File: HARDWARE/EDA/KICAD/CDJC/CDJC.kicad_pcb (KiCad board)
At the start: 2 copper layers, 116.2 x 101.5 mm, 63 parts, among them J1 COM_IN, J2 COM_OUT, J3 POWER_IN, J4 POWER_OUT, J5 BIT_OUT, Q1 BC549, SW1 B-SET, U1 74LS04, U2 74LS32, U3 74LS08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

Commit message: work stop
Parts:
- moved D4 262.7 mm to (-18.7, 256.6), turned to 0 degrees
- moved D5 261.7 mm to (-18.7, 252.4), turned to 0 degrees
- moved D6 260.8 mm to (-18.7, 248.2), turned to 0 degrees
- moved D7 260.0 mm to (-18.7, 244.0), turned to 0 degrees
- moved D8 259.3 mm to (-18.7, 239.8), turned to 0 degrees
- moved U6 256.4 mm to (7.58, 240.5), turned to 0 degrees
- moved R7 245.5 mm to (-6.38, 256.6), turned to 180 degrees
- moved C9 245.3 mm to (15.2, 237.2), turned to 180 degrees
- moved R10 244.4 mm to (-6.38, 252.4), turned to 180 degrees
- moved R12 243.5 mm to (-6.38, 248.2), turned to 180 degrees
- moved R13 242.6 mm to (-6.38, 244.0), turned to 180 degrees
- moved R14 242.0 mm to (-6.38, 239.8), turned to 180 degrees
- moved U8 220.5 mm to (2.93, 208.3), turned to 0 degrees
- moved C3 210.3 mm to (10.6, 205.1), turned to 180 degrees
- moved U7 191.9 mm to (3.78, 177.3), turned to 0 degrees
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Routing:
- net LBLBI: track 87.5 -> 23.2 mm
- net FB_SW: track 68.2 -> 19.4 mm
- net Net-(U1-Pad13): track 44.6 -> 0.00 mm
- net Net-(U1-Pad11): track 44.2 -> 0.00 mm
- net MRI: track 62.2 -> 23.0 mm
- net FBMon: track 37.5 -> 1.13 mm
- net MRLMon: track 29.2 -> 0.00 mm, vias 1 -> 0
- net GNDD: track 168.5 -> 140.0 mm
- net EI: track 50.0 -> 22.9 mm
- net Net-(U1-Pad9): track 26.6 -> 0.00 mm
- net LB_SW: track 34.4 -> 14.8 mm, vias 1 -> 0
- net Net-(U6-Pad11): track 17.7 -> 0.00 mm
- net LBMon: track 17.3 -> 1.04 mm
- net NB_SW: track 40.2 -> 23.9 mm
- net Net-(U6-Pad2): track 9.46 -> 0.00 mm
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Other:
- board size 116.2 x 101.5 mm -> 100 x 100 mm

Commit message: adjust layout pcb
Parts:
- R1, R10, R11, R12, R13, R14, R2, R3, R4, R5, R6, R7, R8, R9: footprint Resistor_THT:R_Axial_DIN0207_L6.3mm_D2.5mm_P7.62mm_Horizontal -> Resistor_THT:R_Axial_DIN0207_L6.3mm_D2.5mm_P2.54mm_Vertical
- moved D4 264.4 mm to (206.0, 117.2), turned to 90 degrees
- moved R7 261.0 mm to (206.0, 104.9), turned to 270 degrees
- moved D5 258.7 mm to (201.8, 117.2), turned to 90 degrees
- moved R10 255.1 mm to (201.8, 104.9), turned to 270 degrees
- moved D6 252.9 mm to (197.6, 117.2), turned to 90 degrees
- moved R12 249.3 mm to (197.6, 104.9), turned to 270 degrees
- moved D7 247.1 mm to (193.4, 117.2), turned to 90 degrees
- moved R13 243.5 mm to (193.4, 104.9), turned to 270 degrees
- moved D8 241.4 mm to (189.2, 117.2), turned to 90 degrees
- moved R14 237.6 mm to (189.2, 104.9), turned to 270 degrees
- moved U6 231.0 mm to (190.9, 99.9), turned to 90 degrees
- moved C7 227.6 mm to (229.0, 76.0), turned to 180 degrees
- moved C9 225.2 mm to (187.6, 92.3), turned to 270 degrees
- moved U9 210.7 mm to (221.3, 80.0), turned to 0 degrees
- moved R1 209.4 mm to (197.2, 64.7)
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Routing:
- net GNDD: track 140.0 -> 88.8 mm
- net FB_SW: track 19.4 -> 2.35 mm
- net NB_SW: track 23.9 -> 13.2 mm
- net LB_SW: track 14.8 -> 9.97 mm
- net LBLBI: track 23.2 -> 19.7 mm
- net Net-(D3-Pad2): track 3.48 -> 0.00 mm
- net Net-(D1-Pad2): track 3.40 -> 0.00 mm
- net MRI: track 23.0 -> 19.7 mm
- net +5VD: track 54.4 -> 51.1 mm
- net EI: track 22.9 -> 19.7 mm
- net Net-(D2-Pad2): track 3.48 -> 0.41 mm
- net Net-(D7-Pad2): track 2.21 -> 0.00 mm
- net Net-(D8-Pad2): track 2.20 -> 0.00 mm
- net Net-(D6-Pad2): track 2.20 -> 0.00 mm
- net Net-(D5-Pad2): track 2.20 -> 0.00 mm
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
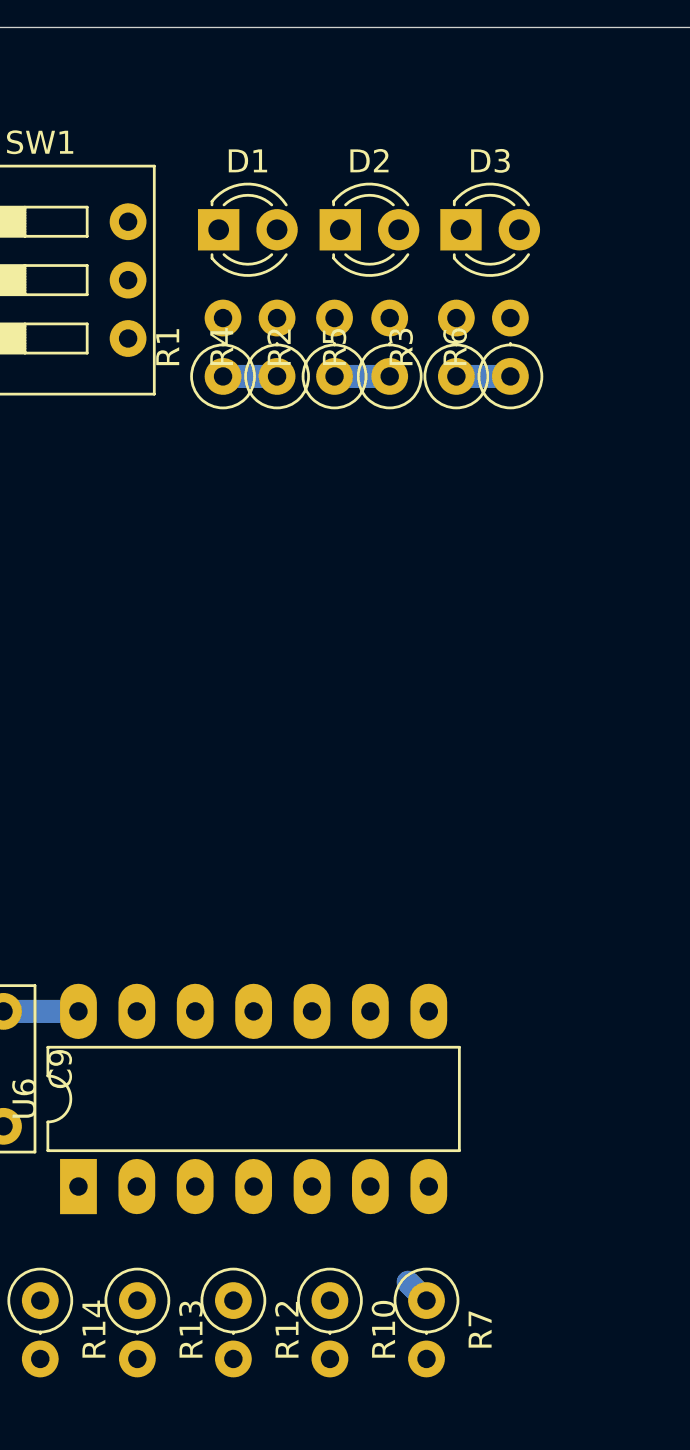
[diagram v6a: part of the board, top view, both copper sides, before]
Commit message: Adjust resitor alingment
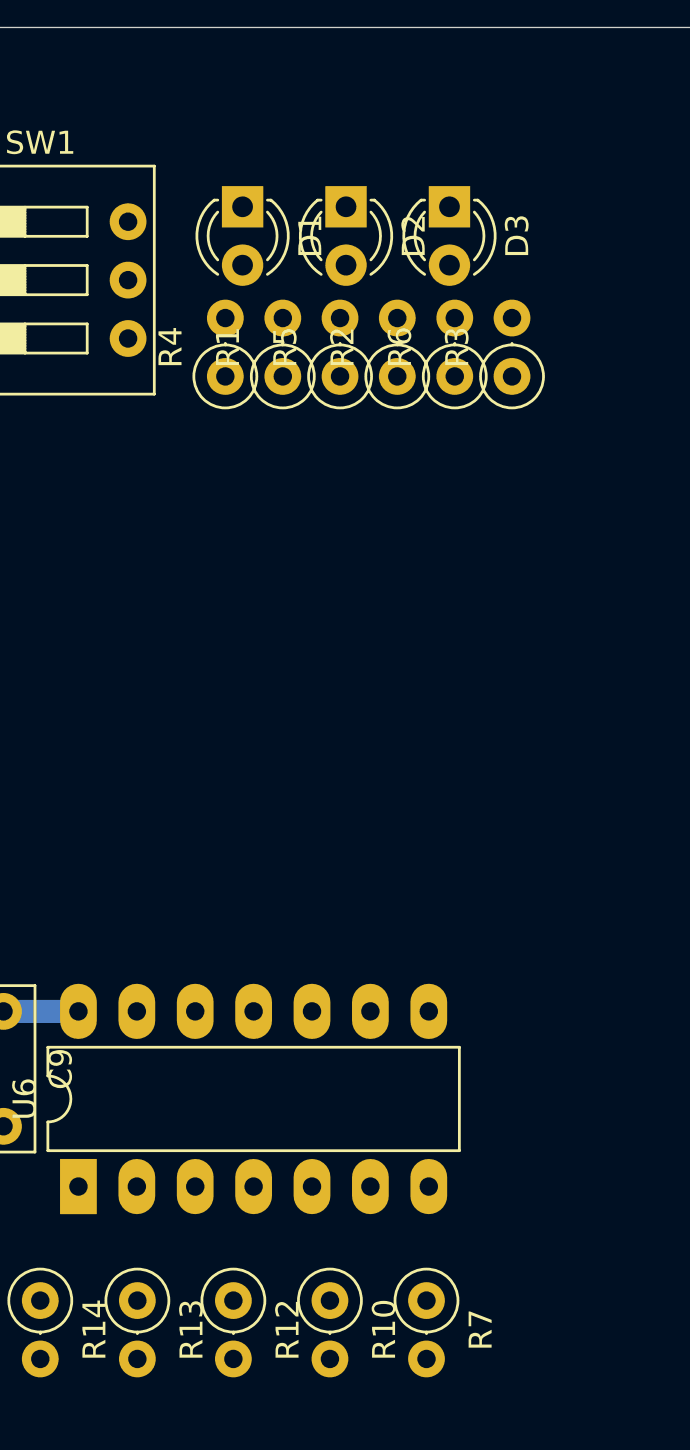
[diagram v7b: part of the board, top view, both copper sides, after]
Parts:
- moved R2 2.73 mm to (204.7, 64.7)
- moved R1 2.60 mm to (199.8, 64.7)
- moved R6 2.42 mm to (207.2, 64.7)
- moved R3 2.42 mm to (209.7, 64.7)
- moved R4 2.25 mm to (197.2, 64.7)
- moved R5 2.16 mm to (202.2, 64.7)
- moved D1 1.44 mm to (198.0, 57.3), turned to 270 degrees
- moved D3 1.12 mm to (207.0, 57.3), turned to 270 degrees
- moved D2 1.03 mm to (202.5, 57.3), turned to 270 degrees
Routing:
- net NB_SW: track 13.2 -> 10.8 mm
- net LB_SW: track 9.97 -> 7.62 mm
- net FB_SW: track 2.35 -> 0.00 mm
- net FBMon: track 1.13 -> 0.00 mm

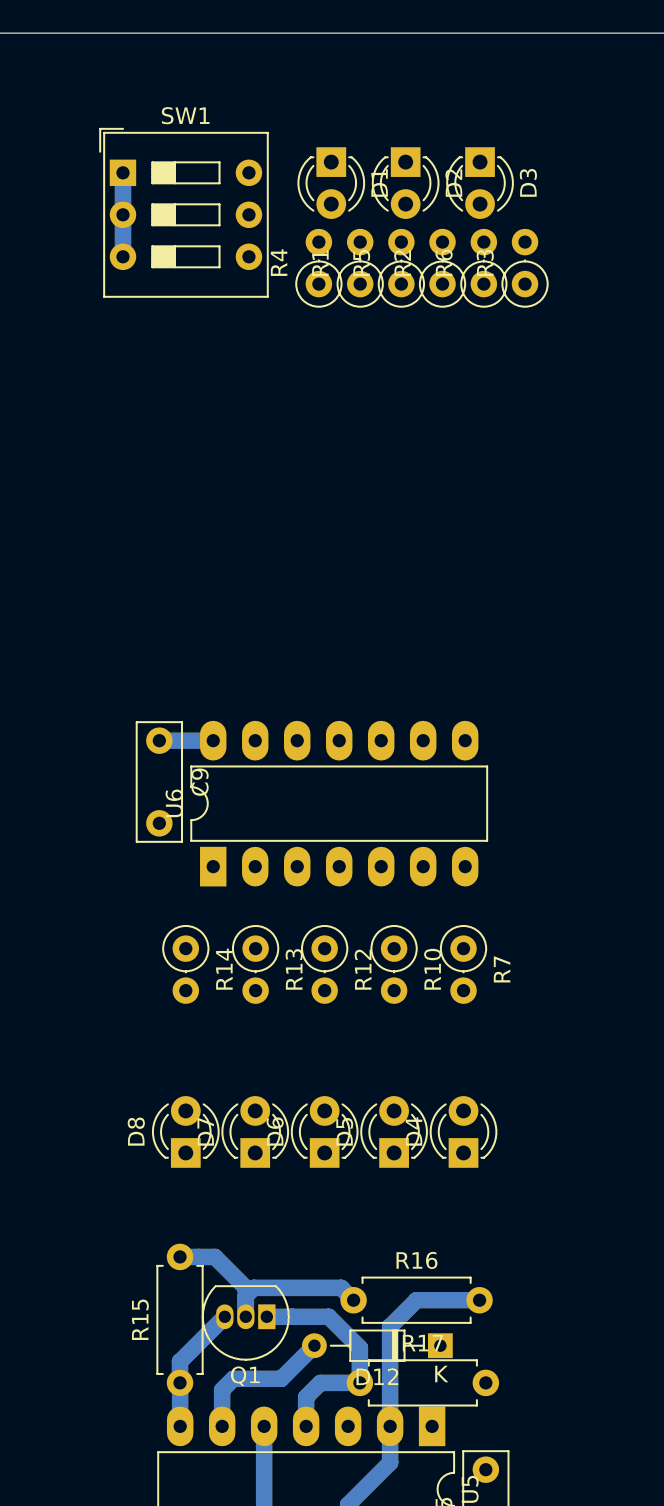
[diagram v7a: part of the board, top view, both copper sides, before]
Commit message: ajust dip and leds mode set
adjust jumper to set mode
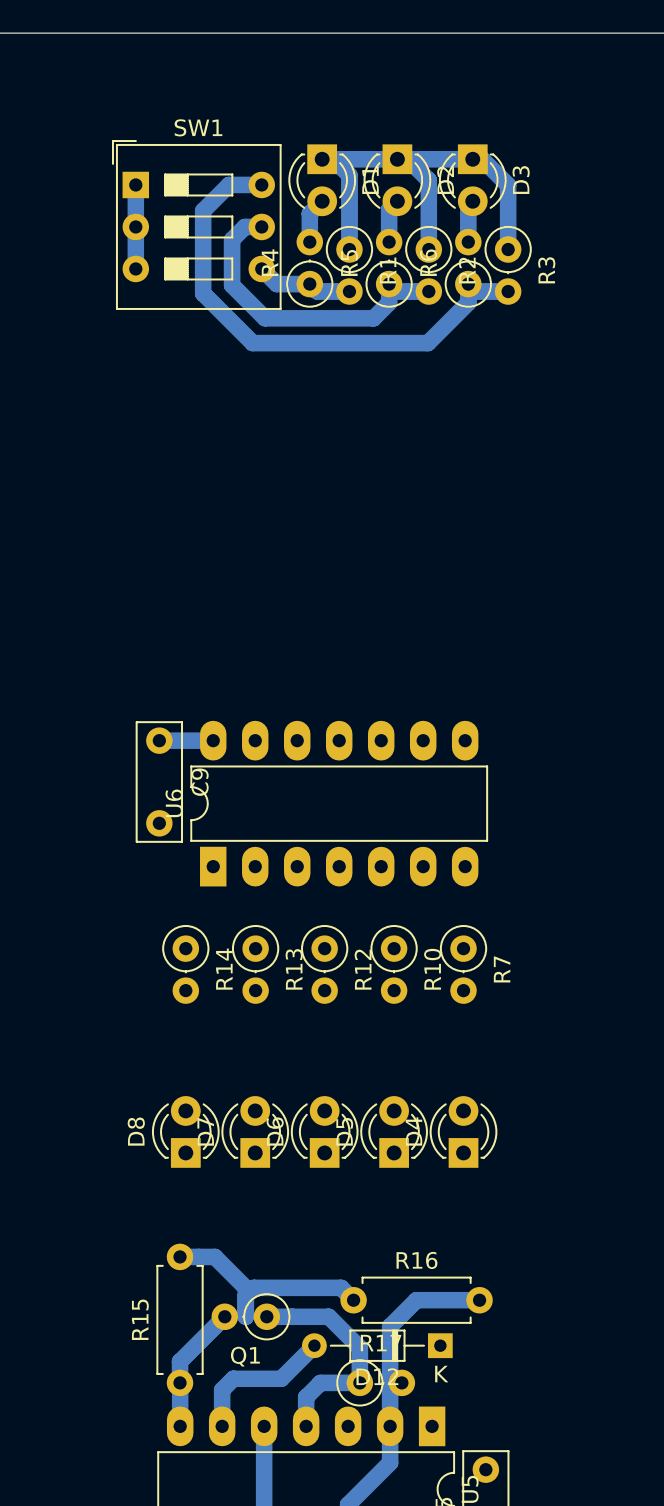
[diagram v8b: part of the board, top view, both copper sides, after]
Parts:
- Q1: footprint Package_TO_SOT_THT:TO-92_Inline -> Resistor_THT:R_Axial_DIN0207_L6.3mm_D2.5mm_P2.54mm_Vertical
- R17: footprint Resistor_THT:R_Axial_DIN0207_L6.3mm_D2.5mm_P7.62mm_Horizontal -> Resistor_THT:R_Axial_DIN0207_L6.3mm_D2.5mm_P2.54mm_Vertical
- moved R3 2.33 mm to (208.7, 62.6), turned to 270 degrees
- moved R2 2.25 mm to (203.9, 62.6), turned to 270 degrees
- moved R1 2.19 mm to (199.1, 62.6), turned to 270 degrees
- moved SW1 1.07 mm to (186.2, 58.7)
- moved R6 0.94 mm to (206.3, 64.7)
- moved R5 0.74 mm to (201.5, 64.7)
- moved D1 0.58 mm to (197.4, 57.1)
- moved R4 0.55 mm to (196.7, 64.7)
- moved D2 0.53 mm to (202.0, 57.1)
- moved D3 0.47 mm to (206.6, 57.1)
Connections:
- R1 pad 1: LB_SW -> GNDD
- R1 pad 2: GNDD -> LB_SW
- R2 pad 1: NB_SW -> GNDD
- R2 pad 2: GNDD -> NB_SW
- R3 pad 1: FB_SW -> GNDD
- R3 pad 2: GNDD -> FB_SW
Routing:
- net FB_SW: track 0.00 -> 31.2 mm
- net GNDD: track 88.7 -> 117.6 mm
- net NB_SW: track 10.8 -> 30.1 mm
- net LB_SW: track 7.62 -> 13.5 mm
- net Net-(D1-Pad2): track 0.00 -> 2.78 mm
- net Net-(D2-Pad2): track 0.00 -> 2.68 mm
- net Net-(D3-Pad2): track 0.00 -> 2.58 mm
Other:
- net class Default: clearance 0.2 -> 0.25
- rule trace_clearance: 0.2 -> 0.25
